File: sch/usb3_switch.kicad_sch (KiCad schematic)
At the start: 31 parts

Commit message: annotated components
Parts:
- gave numbers to parts that had none: 31

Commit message: drc checks and renaming
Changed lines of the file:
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@@
   (junction (at 257.81 80.01) (diameter 0) (color 0 0 0 0)
   )
+  (junction (at 264.16 87.63) (diameter 0) (color 0 0 0 0)
+  )
+  (junction (at 87.63 135.89) (diameter 0) (color 0 0 0 0)
+  )
+  (junction (at 209.55 93.98) (diameter 0) (color 0 0 0 0)
+  )
   (junction (at 139.7 114.3) (diameter 0) (color 0 0 0 0)
-  )
-  (junction (at 264.16 87.63) (diameter 0) (color 0 0 0 0)
-  )
-  (junction (at 87.63 135.89) (diameter 0) (color 0 0 0 0)
-  )
-  (junction (at 209.55 93.98) (diameter 0) (color 0 0 0 0)
   )
   (junction (at 259.08 104.14) (diameter 0) (color 0 0 0 0)
@@
     (pin "8")
   )
+  (symbol (lib_id "power:+3V3") (at 241.3 26.67 0) (unit 1)
+    (in_bom yes) (on_board yes)
+    (property "Reference" "#PWR0130" (id 0) (at 241.3 30.48 0)
+      (effects (font (size 1.27 1.27)) hide)
+    )
+    (property "Value" "+3V3" (id 1) (at 238.76 22.86 0)
+      (effects (font (size 1.27 1.27)) (justify left))
+    )
+    (property "Footprint" "" (id 2) (at 241.3 26.67 0)
+      (effects (font (size 1.27 1.27)) hide)
+    )
+    (property "Datasheet" "" (id 3) (at 241.3 26.67 0)
+      (effects (font (size 1.27 1.27)) hide)
+    )
+    (pin "1")
+  )
   (symbol (lib_id "Device:R") (at 124.46 57.15 0) (unit 1)
     (in_bom yes) (on_board yes) (fields_autoplaced)
@@
     (pin "1")
     (pin "2")
+  )
+  (symbol (lib_id "power:+3V3") (at 139.7 143.51 180) (unit 1)
+    (in_bom yes) (on_board yes)
+    (property "Reference" "#PWR0129" (id 0) (at 139.7 139.7 0)
+      (effects (font (size 1.27 1.27)) hide)
+    )
+    (property "Value" "+3V3" (id 1) (at 142.24 147.32 0)
+      (effects (font (size 1.27 1.27)) (justify left))
+    )
+    (property "Footprint" "" (id 2) (at 139.7 143.51 0)
+      (effects (font (size 1.27 1.27)) hide)
+    )
+    (property "Datasheet" "" (id 3) (at 139.7 143.51 0)
+      (effects (font (size 1.27 1.27)) hide)
+    )
+    (pin "1")
   )
   (symbol (lib_id "power:GND") (at 217.17 97.79 0) (unit 1)
@@
     (pin "2")
   )
-  (symbol (lib_id "power:+3.3V") (at 139.7 114.3 0) (unit 1)
-    (in_bom yes) (on_board yes)
-    (property "Reference" "#PWR055" (id 0) (at 139.7 118.11 0)
-      (effects (font (size 1.27 1.27)) hide)
-    )
-    (property "Value" "+3.3V" (id 1) (at 135.89 110.49 0)
-      (effects (font (size 1.27 1.27)) (justify left))
-    )
-    (property "Footprint" "" (id 2) (at 139.7 114.3 0)
-      (effects (font (size 1.27 1.27)) hide)
-    )
-    (property "Datasheet" "" (id 3) (at 139.7 114.3 0)
+  (symbol (lib_id "power:+3V3") (at 140.97 76.2 0) (unit 1)
+    (in_bom yes) (on_board yes)
+    (property "Reference" "#PWR048" (id 0) (at 140.97 80.01 0)
+      (effects (font (size 1.27 1.27)) hide)
+    )
+    (property "Value" "+3V3" (id 1) (at 140.97 72.39 0))
+    (property "Footprint" "" (id 2) (at 140.97 76.2 0)
+      (effects (font (size 1.27 1.27)) hide)
+    )
+    (property "Datasheet" "" (id 3) (at 140.97 76.2 0)
       (effects (font (size 1.27 1.27)) hide)
     )
@@
     (pin "1")
   )
-  (symbol (lib_id "power:+3.3V") (at 241.3 26.67 0) (unit 1)
-    (in_bom yes) (on_board yes)
-    (property "Reference" "#PWR040" (id 0) (at 241.3 30.48 0)
-      (effects (font (size 1.27 1.27)) hide)
-    )
-    (property "Value" "+3.3V" (id 1) (at 241.3 22.86 0))
-    (property "Footprint" "" (id 2) (at 241.3 26.67 0)
-      (effects (font (size 1.27 1.27)) hide)
-    )
-    (property "Datasheet" "" (id 3) (at 241.3 26.67 0)
-      (effects (font (size 1.27 1.27)) hide)
-    )
-    (pin "1")
-  )
   (symbol (lib_id "Device:R") (at 87.63 130.81 180) (unit 1)
     (in_bom yes) (on_board yes)
@@
     )
     (property "Datasheet" "" (id 3) (at 87.63 135.89 0)
-      (effects (font (size 1.27 1.27)) hide)
-    )
-    (pin "1")
-  )
-  (symbol (lib_id "power:+3.3V") (at 139.7 143.51 180) (unit 1)
-    (in_bom yes) (on_board yes)
-    (property "Reference" "#PWR060" (id 0) (at 139.7 139.7 0)
-      (effects (font (size 1.27 1.27)) hide)
-    )
-    (property "Value" "+3.3V" (id 1) (at 142.24 147.32 0)
-      (effects (font (size 1.27 1.27)) (justify left))
-    )
-    (property "Footprint" "" (id 2) (at 139.7 143.51 0)
-      (effects (font (size 1.27 1.27)) hide)
-    )
-    (property "Datasheet" "" (id 3) (at 139.7 143.51 0)
       (effects (font (size 1.27 1.27)) hide)
     )
@@
     (pin "2")
   )
-  (symbol (lib_id "power:+3.3V") (at 140.97 76.2 0) (unit 1)
-    (in_bom yes) (on_board yes)
-    (property "Reference" "#PWR048" (id 0) (at 140.97 80.01 0)
-      (effects (font (size 1.27 1.27)) hide)
-    )
-    (property "Value" "+3.3V" (id 1) (at 140.97 72.39 0))
-    (property "Footprint" "" (id 2) (at 140.97 76.2 0)
-      (effects (font (size 1.27 1.27)) hide)
-    )
-    (property "Datasheet" "" (id 3) (at 140.97 76.2 0)
-      (effects (font (size 1.27 1.27)) hide)
-    )
+  (symbol (lib_id "power:+3V3") (at 139.7 114.3 0) (unit 1)
+    (in_bom yes) (on_board yes)
+    (property "Reference" "#PWR055" (id 0) (at 139.7 118.11 0)
+      (effects (font (size 1.27 1.27)) hide)
+    )
+    (property "Value" "+3V3" (id 1) (at 138.43 110.49 0))
+    (property "Footprint" "" (id 2) (at 139.7 114.3 0)
+      (effects (font (size 1.27 1.27)) hide)
+    )
+    (property "Datasheet" "" (id 3) (at 139.7 114.3 0)
+      (effects (font (size 1.27 1.27)) hide)
+    )

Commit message: updated power on leds, hub 4 LEDs and misc
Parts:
- R7, R8: value 330Ω -> 330
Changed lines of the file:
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@@
 (kicad_sch (version 20211123) (generator eeschema)
   (paper "A4")
+  (title_block
+    (date "2022-09-12")
+    (rev "0.2")
+    (comment 1 "Runnan Li")
+  )
   (junction (at 257.81 80.01) (diameter 0) (color 0 0 0 0)
   )
@@
       (effects (font (size 1.27 1.27)) (justify left))
     )
-    (property "Value" "330Ω" (id 1) (at 260.35 34.2899 0)
+    (property "Value" "330" (id 1) (at 260.35 34.2899 0)
       (effects (font (size 1.27 1.27)) (justify left))
     )
@@
       (effects (font (size 1.27 1.27)) (justify left))
     )
-    (property "Value" "330Ω" (id 1) (at 269.24 34.2899 0)
-      (effects (font (size 1.27 1.27)) (justify left))
-    )
+    (property "Value" "330" (id 1) (at 269.24 34.2899 0)
+      (effects (font (size 1.27 1.27)) (justify left))
+    )

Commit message: updated 3d models, broken footprints, pcb re-import
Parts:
- MUX1: footprint USB_MUX_DEMUX_PI3USB302-A:USB_MUX_DEMUX_PI3USB302-A -> usb_xwitch:USB_MUX_DEMUX_PI3USB302-A
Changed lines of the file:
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@@
       (effects (font (size 1.27 1.27)) (justify left))
     )
-    (property "Footprint" "USB_MUX_DEMUX_PI3USB302-A:USB_MUX_DEMUX_PI3USB302-A" (id 2) (at 142.24 129.54 0)
+    (property "Footprint" "usb_xwitch:USB_MUX_DEMUX_PI3USB302-A" (id 2) (at 142.24 129.54 0)
       (effects (font (size 1.27 1.27)) hide)
     )

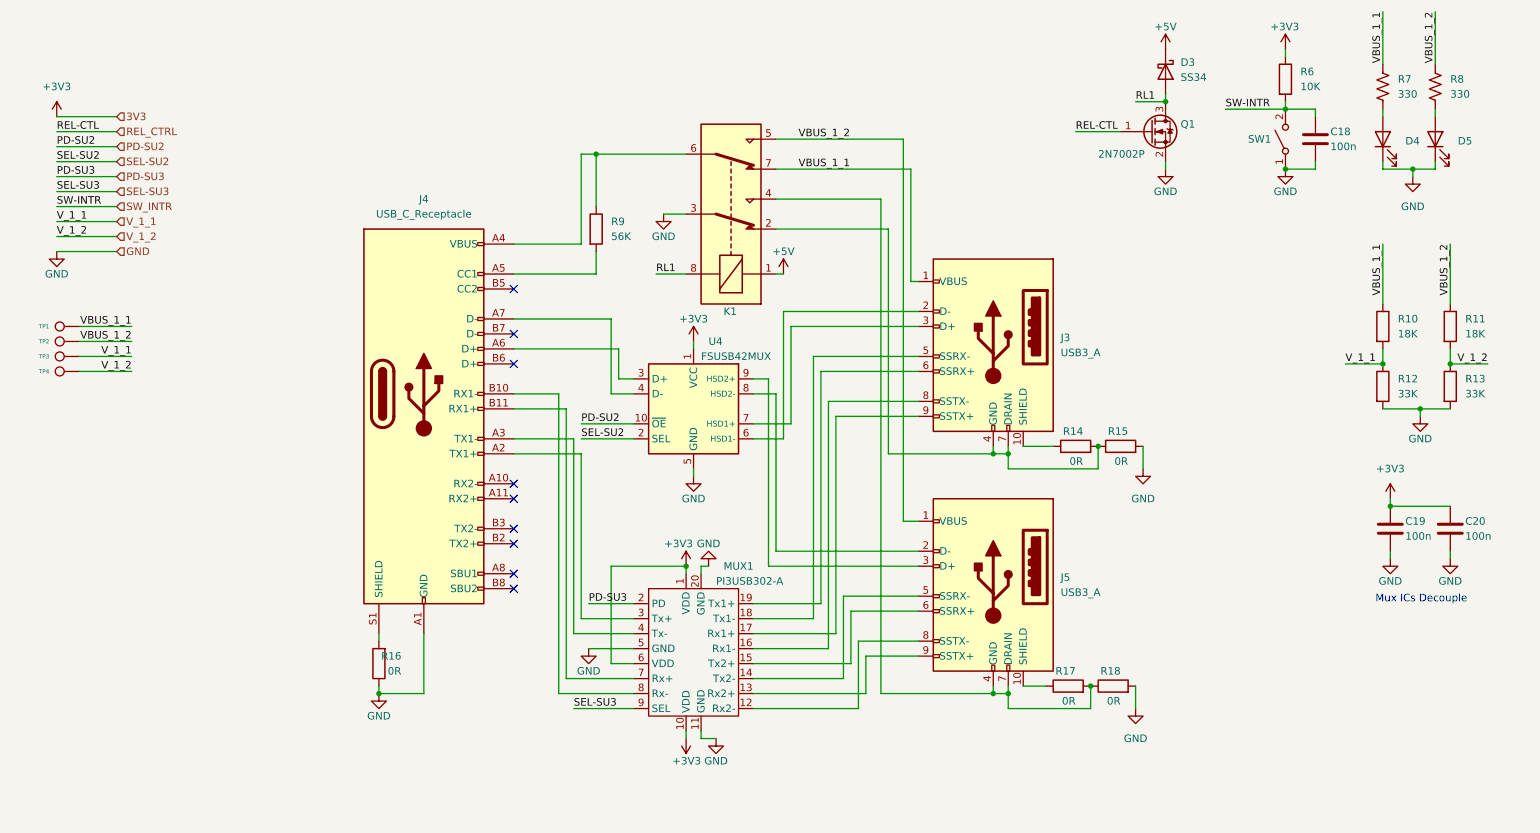
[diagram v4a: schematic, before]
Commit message: update label for easy routing differential pair
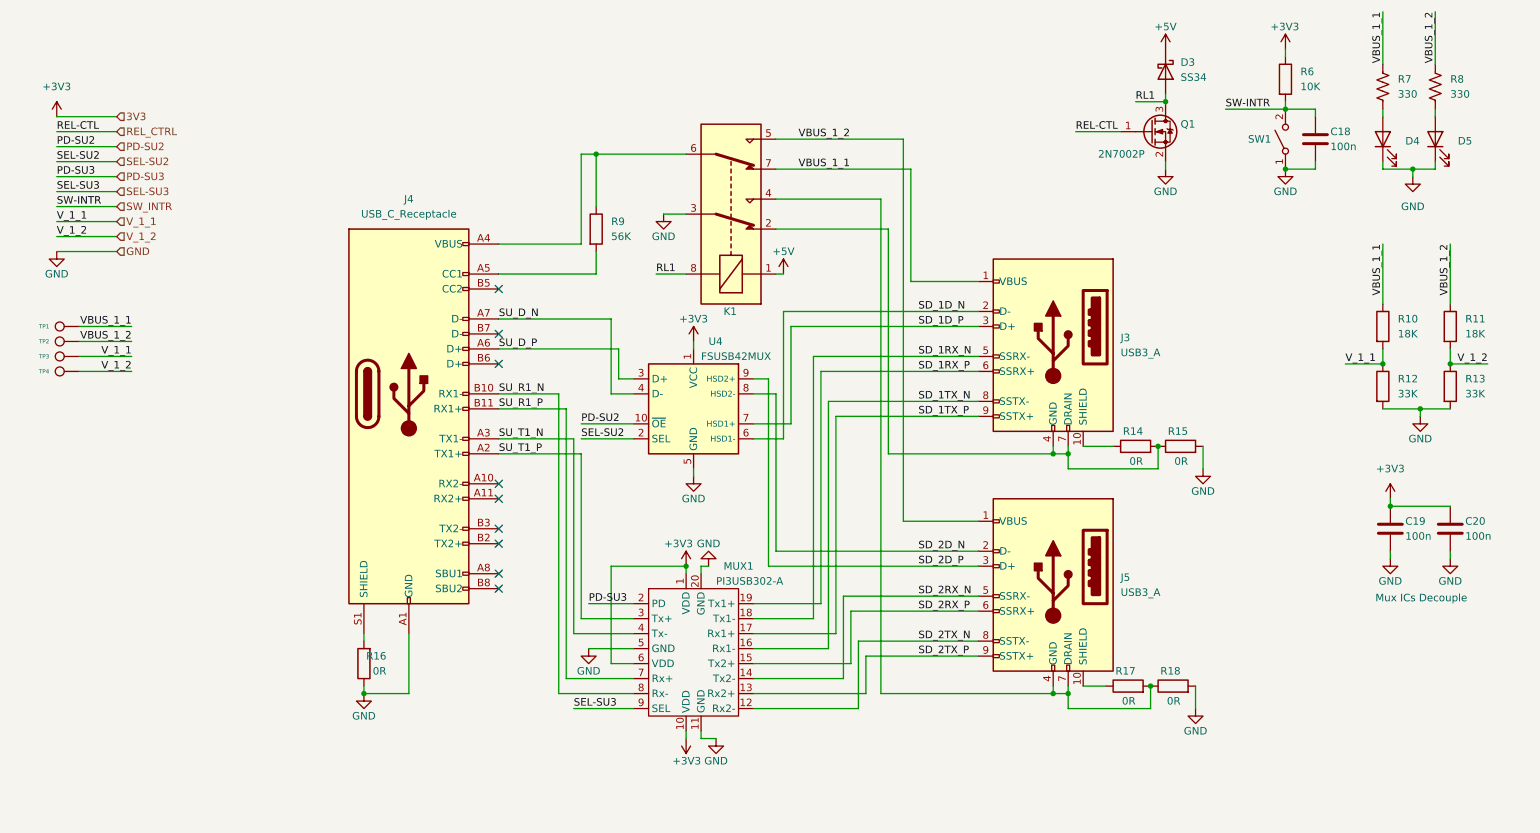
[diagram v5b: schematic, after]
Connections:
- net SU_T1_P: now reaches J4.A2 (TX1+), MUX1.3 (Tx+)
- net SU_T1_N: now reaches J4.A3 (TX1-), MUX1.4 (Tx-)
- net SU_D_P: now reaches J4.A6 (D+), U4.3 (D+)
- net SU_D_N: now reaches J4.A7 (D-), U4.4 (D-)
- net SU_R1_N: now reaches J4.B10 (RX1-), MUX1.8 (Rx-)
- net SU_R1_P: now reaches J4.B11 (RX1+), MUX1.7 (Rx+)
- net SD_1D_N: now reaches J3.2 (D-), U4.6 (HSD1-)
- net SD_1D_P: now reaches J3.3 (D+), U4.7 (HSD1+)
- net SD_1RX_N: now reaches J3.5 (SSRX-), MUX1.18 (Tx1-)
- net SD_1RX_P: now reaches J3.6 (SSRX+), MUX1.19 (Tx1+)
- net SD_1TX_N: now reaches J3.8 (SSTX-), MUX1.16 (Rx1-)
- net SD_1TX_P: now reaches J3.9 (SSTX+), MUX1.17 (Rx1+)
- net SD_2D_N: now reaches J5.2 (D-), U4.8 (HSD2-)
- net SD_2D_P: now reaches J5.3 (D+), U4.9 (HSD2+)
- net SD_2RX_N: now reaches J5.5 (SSRX-), MUX1.14 (Tx2-)
- net SD_2RX_P: now reaches J5.6 (SSRX+), MUX1.15 (Tx2+)
- net SD_2TX_N: now reaches J5.8 (SSTX-), MUX1.12 (Rx2-)
- net SD_2TX_P: now reaches J5.9 (SSTX+), MUX1.13 (Rx2+)
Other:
- moved on the sheet: J3, J4, J5, R14, R15, R16, R17, R18

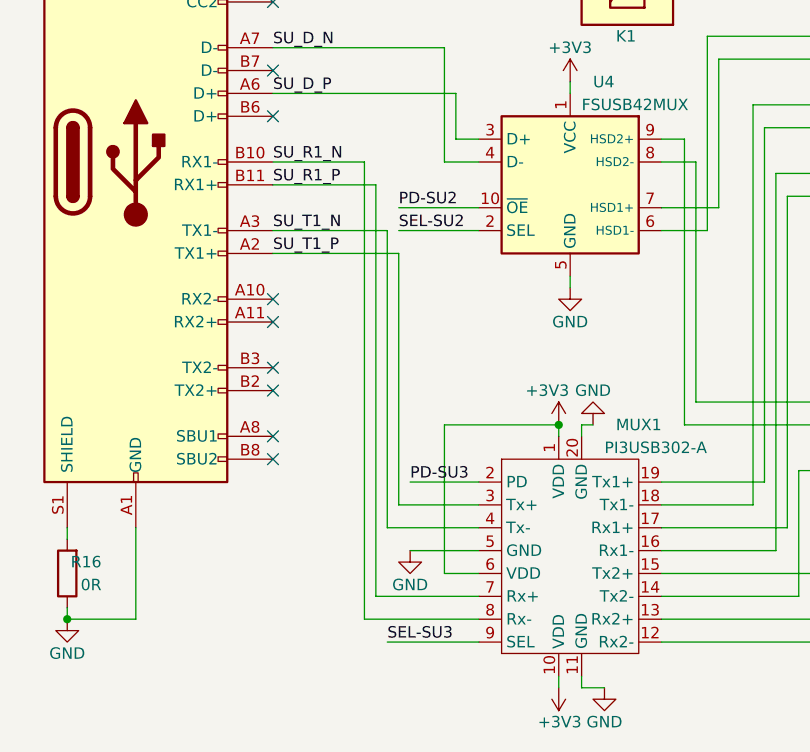
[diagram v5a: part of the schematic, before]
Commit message: wrong wiring fixed on usb switch; update layout
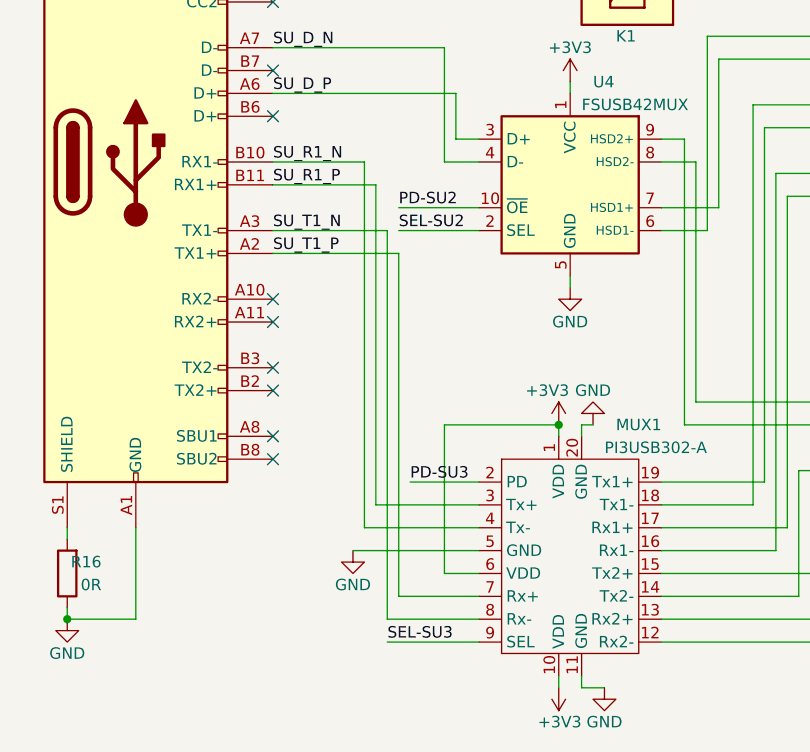
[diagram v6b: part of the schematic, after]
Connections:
- net SU_R1_N: now also MUX1.4 (Tx-); no longer MUX1.8 (Rx-)
- net SU_R1_P: now also MUX1.3 (Tx+); no longer MUX1.7 (Rx+)
- net SU_T1_N: now also MUX1.8 (Rx-); no longer MUX1.4 (Tx-)
- net SU_T1_P: now also MUX1.7 (Rx+); no longer MUX1.3 (Tx+)
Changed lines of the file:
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@@
-    (stroke (width 0) (type default) (color 0 0 0 0))
-  )
-  (wire (pts (xy 119.38 87.63) (xy 119.38 133.35))
     (stroke (width 0) (type default) (color 0 0 0 0))
   )
@@
     (stroke (width 0) (type default) (color 0 0 0 0))
   )
-  (wire (pts (xy 120.65 125.73) (xy 130.81 125.73))
-    (stroke (width 0) (type default) (color 0 0 0 0))
-  )
   (wire (pts (xy 246.38 38.1) (xy 246.38 36.83))
     (stroke (width 0) (type default) (color 0 0 0 0))
@@
     (stroke (width 0) (type default) (color 0 0 0 0))
   )
+  (wire (pts (xy 120.65 92.71) (xy 120.65 135.89))
+    (stroke (width 0) (type default) (color 0 0 0 0))
+  )
   (wire (pts (xy 257.81 59.69) (xy 257.81 69.85))
     (stroke (width 0) (type default) (color 0 0 0 0))
@@
     (stroke (width 0) (type default) (color 0 0 0 0))
   )
-  (wire (pts (xy 121.92 95.25) (xy 121.92 123.19))
-    (stroke (width 0) (type default) (color 0 0 0 0))
-  )
   (wire (pts (xy 107.95 77.47) (xy 128.27 77.47))
     (stroke (width 0) (type default) (color 0 0 0 0))
@@
     (stroke (width 0) (type default) (color 0 0 0 0))
   )
+  (wire (pts (xy 121.92 133.35) (xy 130.81 133.35))
+    (stroke (width 0) (type default) (color 0 0 0 0))
+  )
   (wire (pts (xy 173.99 95.25) (xy 201.93 95.25))
     (stroke (width 0) (type default) (color 0 0 0 0))
@@
     (stroke (width 0) (type default) (color 0 0 0 0))
   )
-  (wire (pts (xy 118.11 135.89) (xy 130.81 135.89))
-    (stroke (width 0) (type default) (color 0 0 0 0))
-  )
   (wire (pts (xy 257.81 20.32) (xy 257.81 29.21))
     (stroke (width 0) (type default) (color 0 0 0 0))
@@
     (stroke (width 0) (type default) (color 0 0 0 0))
   )
-  (wire (pts (xy 120.65 92.71) (xy 120.65 125.73))
+  (wire (pts (xy 121.92 95.25) (xy 121.92 133.35))
     (stroke (width 0) (type default) (color 0 0 0 0))
   )
@@
     (stroke (width 0) (type default) (color 0 0 0 0))
   )
-  (wire (pts (xy 118.11 85.09) (xy 118.11 135.89))
-    (stroke (width 0) (type default) (color 0 0 0 0))
-  )
-  (wire (pts (xy 123.19 128.27) (xy 130.81 128.27))
+  (wire (pts (xy 116.84 128.27) (xy 130.81 128.27))
+    (stroke (width 0) (type default) (color 0 0 0 0))
+  )
+  (wire (pts (xy 118.11 125.73) (xy 130.81 125.73))
     (stroke (width 0) (type default) (color 0 0 0 0))
   )
@@
     (stroke (width 0) (type default) (color 0 0 0 0))
   )
+  (wire (pts (xy 120.65 135.89) (xy 130.81 135.89))
+    (stroke (width 0) (type default) (color 0 0 0 0))
+  )
   (wire (pts (xy 151.13 123.19) (xy 161.29 123.19))
     (stroke (width 0) (type default) (color 0 0 0 0))
@@
     (stroke (width 0) (type default) (color 0 0 0 0))
   )
+  (wire (pts (xy 119.38 123.19) (xy 130.81 123.19))
+    (stroke (width 0) (type default) (color 0 0 0 0))
+  )
   (wire (pts (xy 275.59 80.01) (xy 269.24 80.01))
     (stroke (width 0) (type default) (color 0 0 0 0))
@@
     (stroke (width 0) (type default) (color 0 0 0 0))
   )
-  (wire (pts (xy 121.92 123.19) (xy 130.81 123.19))
-    (stroke (width 0) (type default) (color 0 0 0 0))
-  )
   (wire (pts (xy 269.24 59.69) (xy 269.24 69.85))
     (stroke (width 0) (type default) (color 0 0 0 0))
@@
     (stroke (width 0) (type default) (color 0 0 0 0))
   )
+  (wire (pts (xy 118.11 85.09) (xy 118.11 125.73))
+    (stroke (width 0) (type default) (color 0 0 0 0))
+  )
   (wire (pts (xy 218.44 138.43) (xy 204.47 138.43))
     (stroke (width 0) (type default) (color 0 0 0 0))
@@
     (stroke (width 0) (type default) (color 0 0 0 0))
   )
+  (wire (pts (xy 119.38 87.63) (xy 119.38 123.19))
+    (stroke (width 0) (type default) (color 0 0 0 0))
+  )
   (wire (pts (xy 92.71 125.73) (xy 92.71 135.89))
     (stroke (width 0) (type default) (color 0 0 0 0))
@@
   )
   (wire (pts (xy 269.24 111.76) (xy 269.24 113.03))
-    (stroke (width 0) (type default) (color 0 0 0 0))
-  )
-  (wire (pts (xy 119.38 133.35) (xy 130.81 133.35))
     (stroke (width 0) (type default) (color 0 0 0 0))
   )
@@
     (pin "1")
   )
-  (symbol (lib_id "power:GND") (at 123.19 128.27 0) (unit 1)
-    (in_bom yes) (on_board yes)
-    (property "Reference" "#PWR057" (id 0) (at 123.19 134.62 0)
-      (effects (font (size 1.27 1.27)) hide)
-    )
-    (property "Value" "GND" (id 1) (at 123.19 132.08 0))
-    (property "Footprint" "" (id 2) (at 123.19 128.27 0)
-      (effects (font (size 1.27 1.27)) hide)
-    )
-    (property "Datasheet" "" (id 3) (at 123.19 128.27 0)
-      (effects (font (size 1.27 1.27)) hide)
-    )
+  (symbol (lib_id "power:GND") (at 116.84 128.27 0) (unit 1)
+    (in_bom yes) (on_board yes)
+    (property "Reference" "#PWR057" (id 0) (at 116.84 134.62 0)
+      (effects (font (size 1.27 1.27)) hide)
+    )
+    (property "Value" "GND" (id 1) (at 116.84 132.08 0))
+    (property "Footprint" "" (id 2) (at 116.84 128.27 0)
+      (effects (font (size 1.27 1.27)) hide)
+    )
+    (property "Datasheet" "" (id 3) (at 116.84 128.27 0)
+      (effects (font (size 1.27 1.27)) hide)
+    )

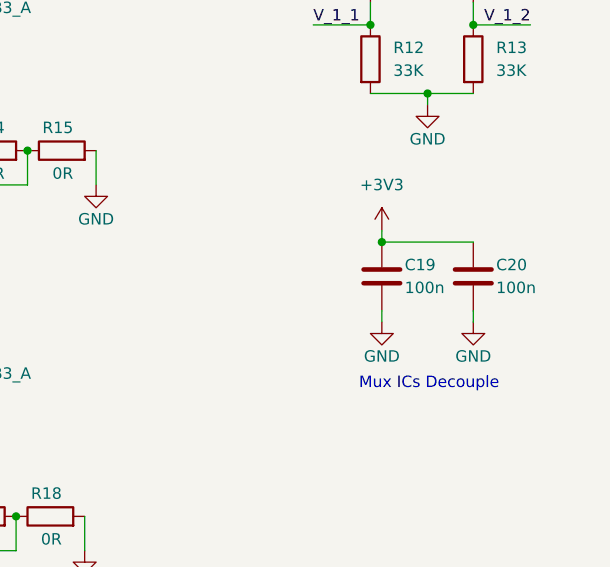
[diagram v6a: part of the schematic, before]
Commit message: updated usb layout
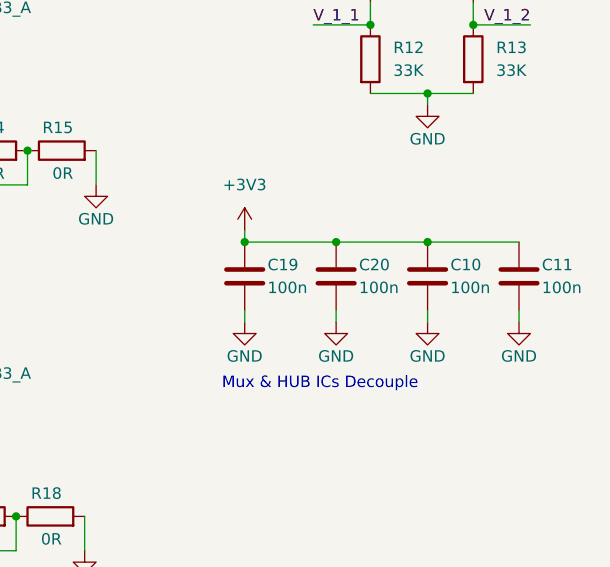
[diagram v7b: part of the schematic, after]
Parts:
- added C10, C11: 100n, Resistor_SMD:R_0402_1005Metric_Pad0.72x0.64mm_HandSolder, symbol Device:C
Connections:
- net +3V3: now also C10.1, C11.1
- net GND: now also C10.2, C11.2
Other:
- note added: "Mux & HUB ICs Decouple"
- note removed: "Mux ICs Decouple"
- moved on the sheet: C19, C20
